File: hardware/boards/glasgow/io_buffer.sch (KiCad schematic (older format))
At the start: 63 parts, among them J2 Conn_02x10_Odd_Even, J6 Conn_01x08, J7 Conn_01x08, U10 DAC081C081CIMK, U11 TPS73101DBV, U16 SN74LVC1T45DRL, U17 SN74LVC1T45DRL, U18 SN74LVC1T45DRL, U19 PCA6408APW, U19 SN74LVC1T45DRL, U20 SN74LVC1T45DRL, U21 INA233, U21 SN74LVC1T45DRL, U5 SN74LVC1T45DRL, U6 SN74LVC1T45DRL

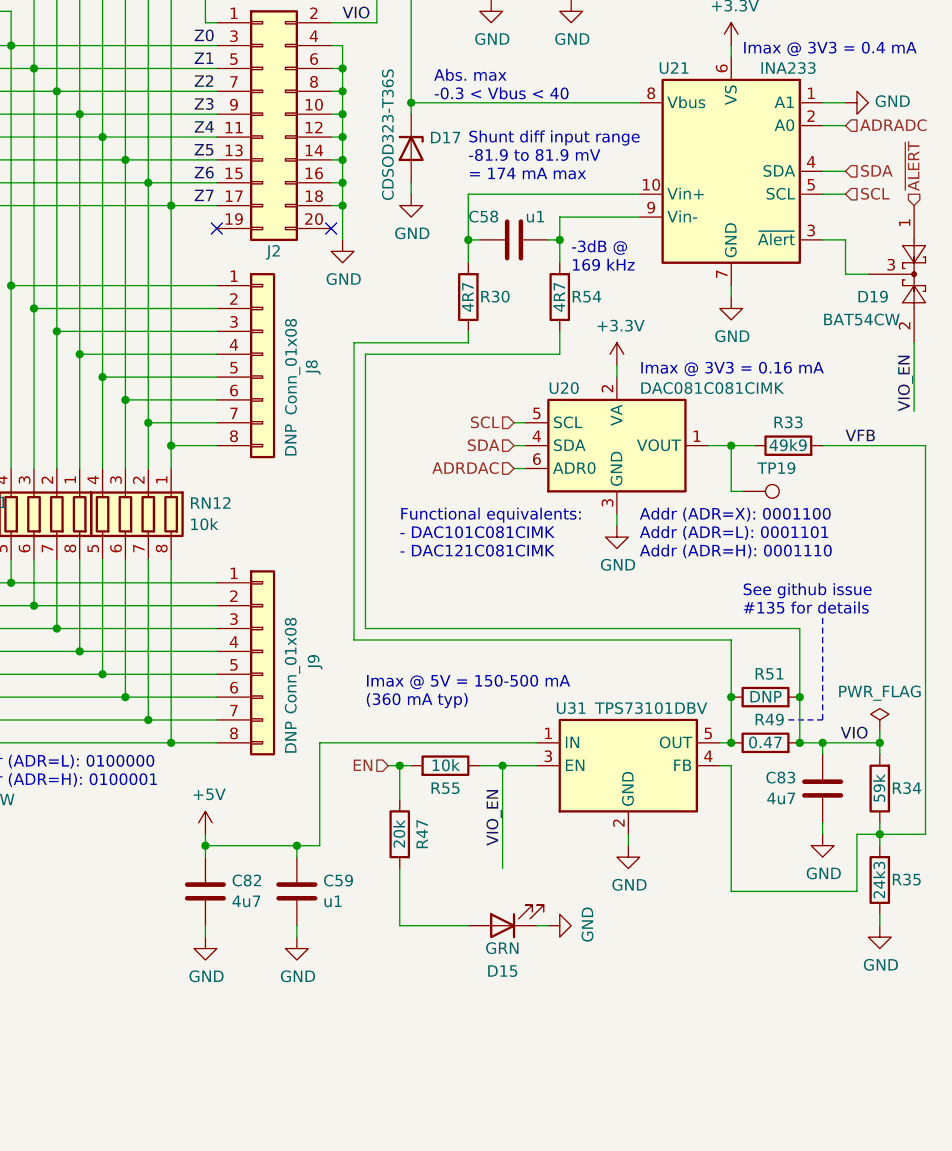
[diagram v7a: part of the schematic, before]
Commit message: revC2: separate current shunt for the INA233
The original idea in #165 and #135 was to reuse the 0.47 Ohms dropper resistor
we already have for the regulator as current shunt too. As the INA233 has a fixed
measurement range of +- 81.9 mV, this would allow to measure 174 mA. My initial
thought was that this is enough, as the specced load of the TPS73101 is 150 mA.

Review and experimentation has shown that the TPS73101 can be used to 350 mA in
most configurations before limiting set in, for a programmed output of 5 V I
could use it even up to 420 mA. As one of the design goals of using the INA233
is overcurrent protection, the settable range should be higher than what the
regulator can output in best case.

So the design is changed to a 0.15 Ohms current shunt and an additional 0.33 Ohms
dropper resistor in series. This gives a total 0.48 Ohms drop for the regulator
and a measurable current range to 546 mA.

For both resistors a DNPed parallel footprint is provided as before, allowing
the user to reduce the voltage drop if desired.
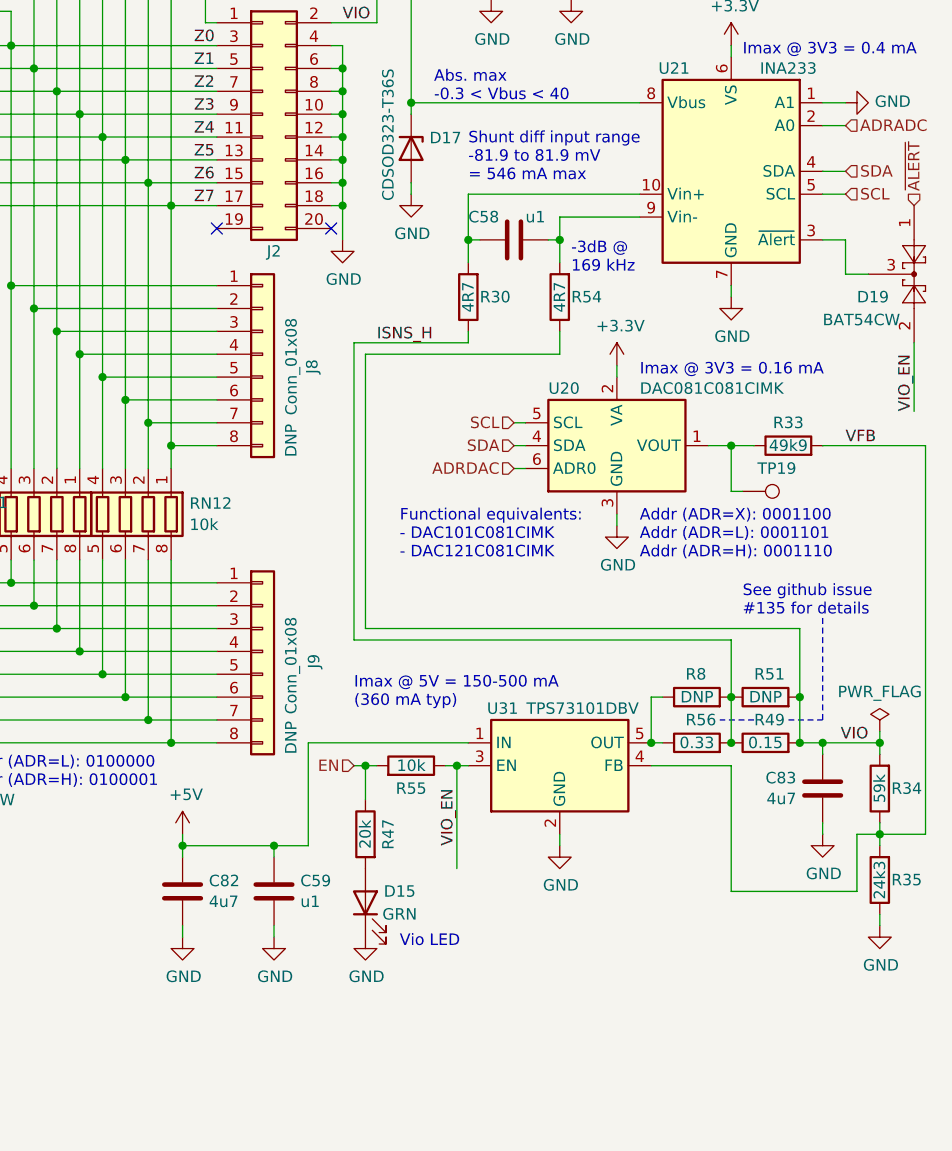
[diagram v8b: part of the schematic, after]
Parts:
- added R56: 0.33, Resistor_SMD:R_0603_1608Metric, symbol Device:R
- added R8: DNP, Resistor_SMD:R_0603_1608Metric, symbol Device:R
- R49: value 0.47 -> 0.15; 1b2-bom-key res-0603-0_47 -> res-0603-0_15; MPN CRL0603-JW-R470ELF -> KDV06FR150ET; Mfg Bourns -> Ohmite
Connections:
- net ISNS_H: now reaches R30.1, R49.1, R51.1
- net ISNS_H: now also R56.2, R8.2; no longer U11.5 (OUT)
- new net: R56.1, R8.1, U11.5 (OUT)
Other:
- note added: "Shunt diff input range\n-81.9 to 81.9 mV\n= 546 mA max"
- note added: "Vio LED"
- note removed: "Shunt diff input range\n-81.9 to 81.9 mV\n= 174 mA max"
- moved on the sheet: C59, C82, D15, R47, R55, U31
